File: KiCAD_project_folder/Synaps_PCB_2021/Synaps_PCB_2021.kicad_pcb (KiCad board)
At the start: 4 copper layers, 101.6 x 101.6 mm, 75 parts, among them IC2 ESP32-S2, J1 USB_C_Receptacle, J2 Conn_01x20_MountingPin, J3 Conn_01x20_MountingPin, Q2 Q_PMOS_DGS, SW2 SW_Push, SW3 SW_Push, SW4 SW_Push, U1 MAX14748BEWW+, U2 CD74HC4067M, U3 AT25DF041x-UxN-x, Y2 Crystal_GND24, Y3 32.768K

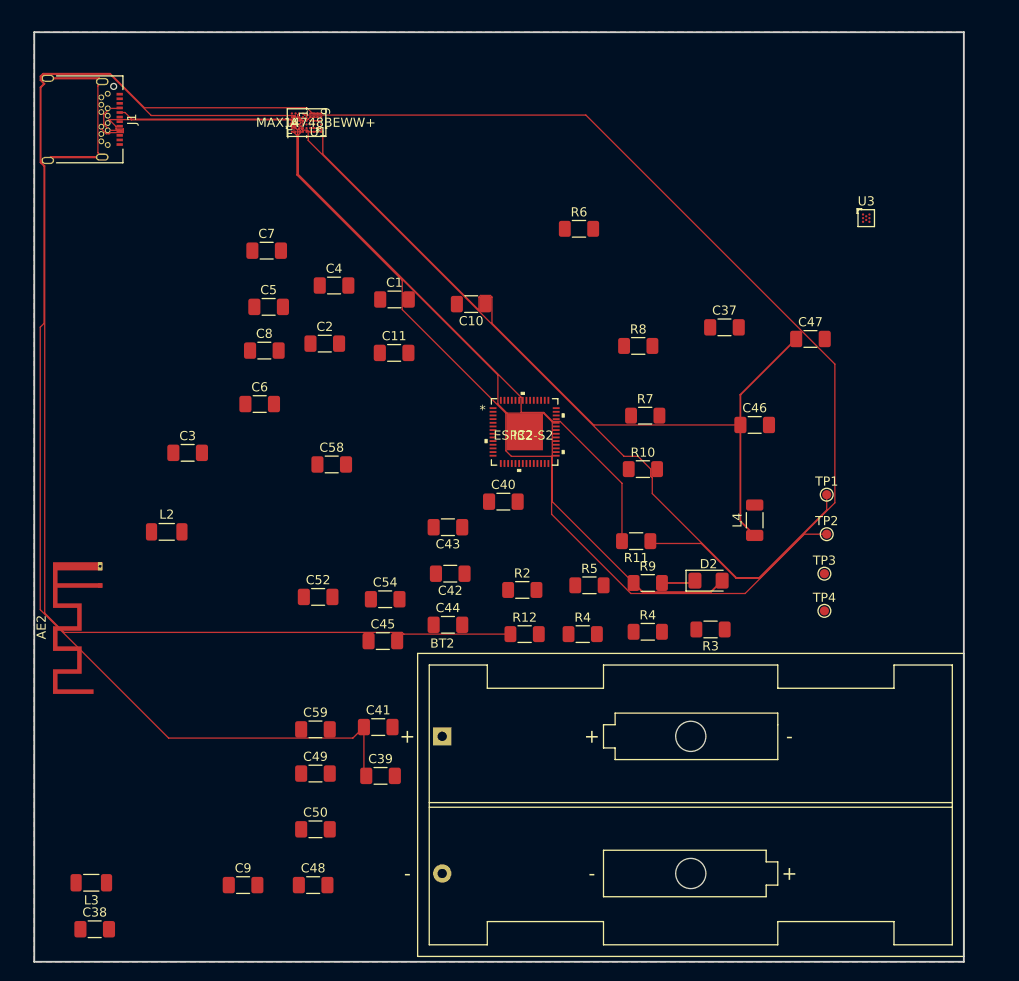
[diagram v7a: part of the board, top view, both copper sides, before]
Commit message: Fixed missing connections + plus added rough BOM
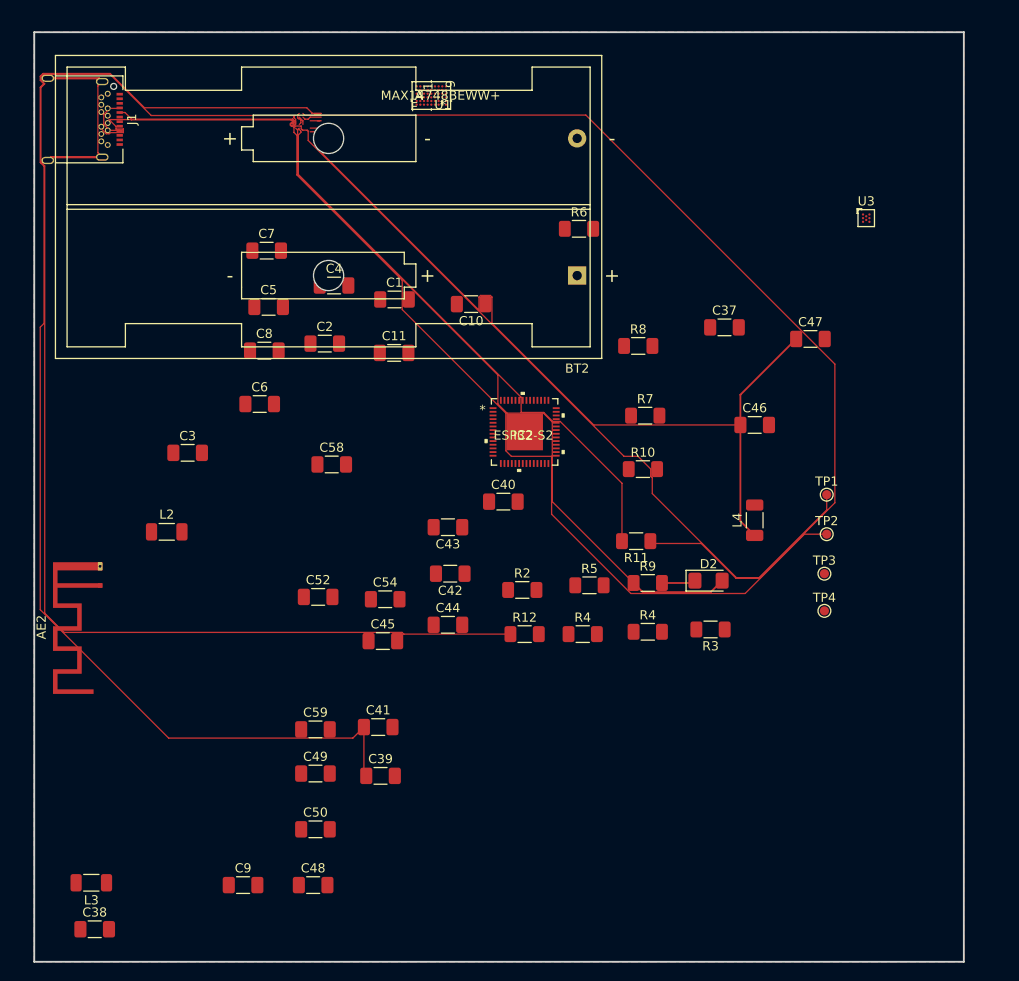
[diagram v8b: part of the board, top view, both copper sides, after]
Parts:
- moved BT2 52.5 mm to (154.1, 73.6), turned to 180 degrees
- moved U1 14.0 mm to (138.1, 53.9)
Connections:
- C1 pad 1: unconnected-(C1-Pad1) -> VBUS
- IC2 pad 16: /Microcontroler/GPIO11 -> /Connectors/GPIO11
- IC2 pad 28: /Microcontroler/GPIO21 -> /Connectors/GPIO11
- J1 pad A4: /Power Supply/CHGIN -> VBUS
- J1 pad A9: /Power Supply/CHGIN -> VBUS
- J1 pad B4: /Power Supply/CHGIN -> VBUS
- J1 pad B9: /Power Supply/CHGIN -> VBUS
- J3 pad 10: /Probes schematic/SPI_OUT_ADC3 -> /Probes schematic/SPI_CS_ADC3
- J3 pad 11: /Probes schematic/SPI_CS_ADC4 -> /Probes schematic/SPI_OUT_ADC3
- J3 pad 12: /Probes schematic/SPI_OUT_ADC4 -> /Probes schematic/SPI_CS_ADC4
- J3 pad 13: /Probes schematic/SPI_CS_ADC5 -> /Probes schematic/SPI_OUT_ADC4
- J3 pad 14: /Probes schematic/SPI_OUT_ADC5 -> /Probes schematic/SPI_CS_ADC5
- J3 pad 15: /Probes schematic/SPI_CS_ADC6 -> /Probes schematic/SPI_OUT_ADC5
- J3 pad 16: /Probes schematic/SPI_OUT_ADC6 -> /Probes schematic/SPI_CS_ADC6
- J3 pad 17: /Probes schematic/SPI_CS_ADC7 -> /Probes schematic/SPI_OUT_ADC6
- J3 pad 18: /Probes schematic/SPI_OUT_ADC7 -> /Probes schematic/SPI_CS_ADC7
- J3 pad 19: GNDREF -> /Probes schematic/SPI_OUT_ADC7
- J3 pad 3: /Probes schematic/SPI_CS_ADC0 -> /Microcontroler/SPI3_MOSI
- J3 pad 4: /Probes schematic/SPI_OUT_ADC0 -> /Probes schematic/SPI_CS_ADC0
- J3 pad 5: /Probes schematic/SPI_CS_ADC1 -> /Probes schematic/SPI_OUT_ADC0
- J3 pad 6: /Probes schematic/SPI_OUT_ADC1 -> /Probes schematic/SPI_CS_ADC1
- J3 pad 7: /Probes schematic/SPI_CS_ADC2 -> /Probes schematic/SPI_OUT_ADC1
- J3 pad 8: /Probes schematic/SPI_OUT_ADC2 -> /Probes schematic/SPI_CS_ADC2
- J3 pad 9: /Probes schematic/SPI_CS_ADC3 -> /Probes schematic/SPI_OUT_ADC2
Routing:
- net VBUS: track 0.00 -> 5.42 mm
- net /Power Supply/CHGIN: track 5.42 -> 0.00 mm
- net Net-(C46-Pad1): track 90.8 -> 92.0 mm
- net Net-(Q2-Pad3): track 1.20 -> 0.00 mm
